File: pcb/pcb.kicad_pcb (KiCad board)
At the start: 2 copper layers, 57 parts, among them J1 AMT0440007DB0000G, J10 Conn_02x10_Counter_Clockwise, J11 Conn_01x03, J12 Conn_01x02, J15 Conn_01x10, J16 Conn_01x10, J2 AMT0440007DB0000G, J3 AMT0440007DB0000G, J4 AMT0440007DB0000G, J5 Conn_01x03, J6 Conn_01x03, J7 Conn_01x03, J8 Conn_01x03, J9 Conn_01x03, Q1 IRF9Z34NPBF, Q2 IRF9Z34NPBF, Q3 IRF9Z34NPBF, Q4 IRF9Z34NPBF, Q5 IRF9Z34NPBF, U1 ACS711ELCTR-12AB-T, U2 ACS711ELCTR-12AB-T, U3 ACS711ELCTR-12AB-T, U4 ACS711ELCTR-12AB-T, U5 ACS711ELCTR-12AB-T, U6 TXS0102DCUR, U7 TXS0102DCUR, U8 TXS0102DCUR, U9 NCP718BSNADJT1G

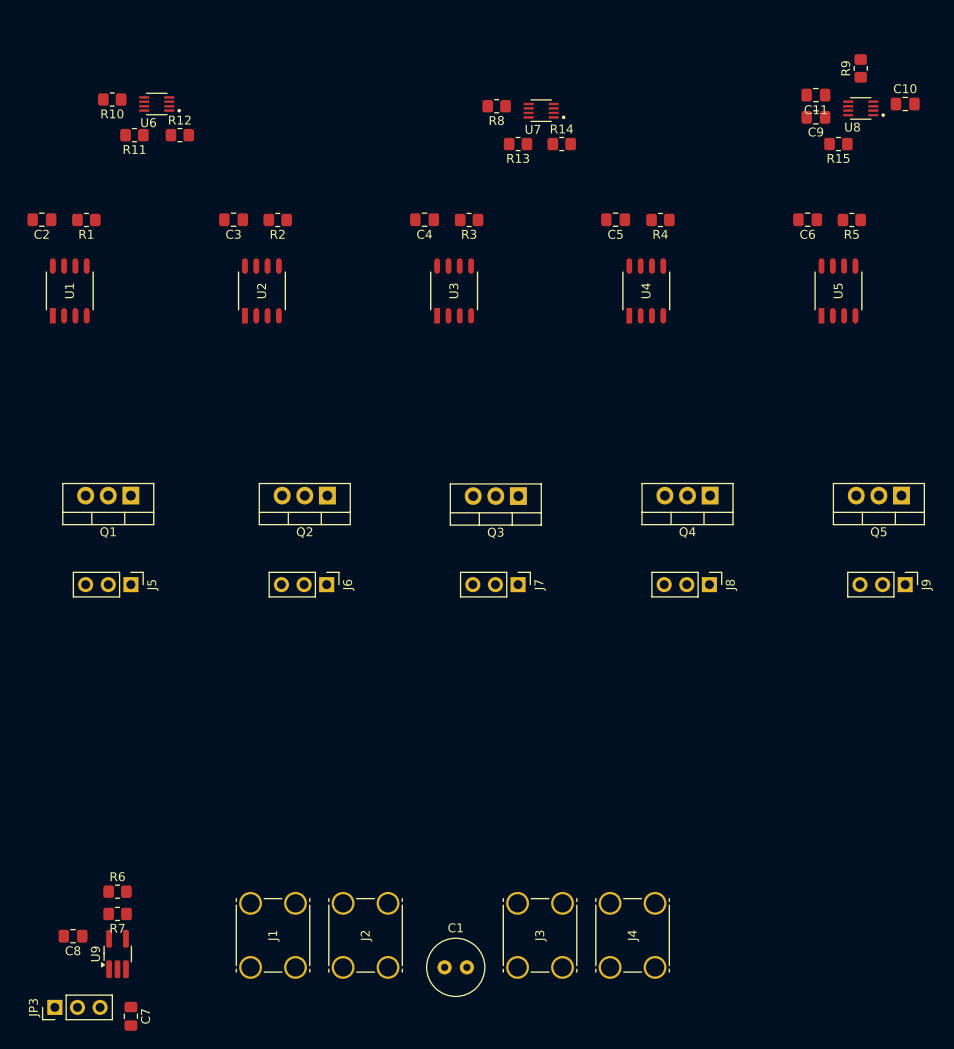
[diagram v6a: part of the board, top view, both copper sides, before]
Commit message: Add bypass capacitors for each level shifter
The datasheet for the level shifter recommends placing the bypass
capacitors as close as possible to the IC. Ideally, we could probably
get away with just the one set. However, since the level shifters are
placed so far away from each other, it's probably better to have more
caps and slightly higher capacicance.
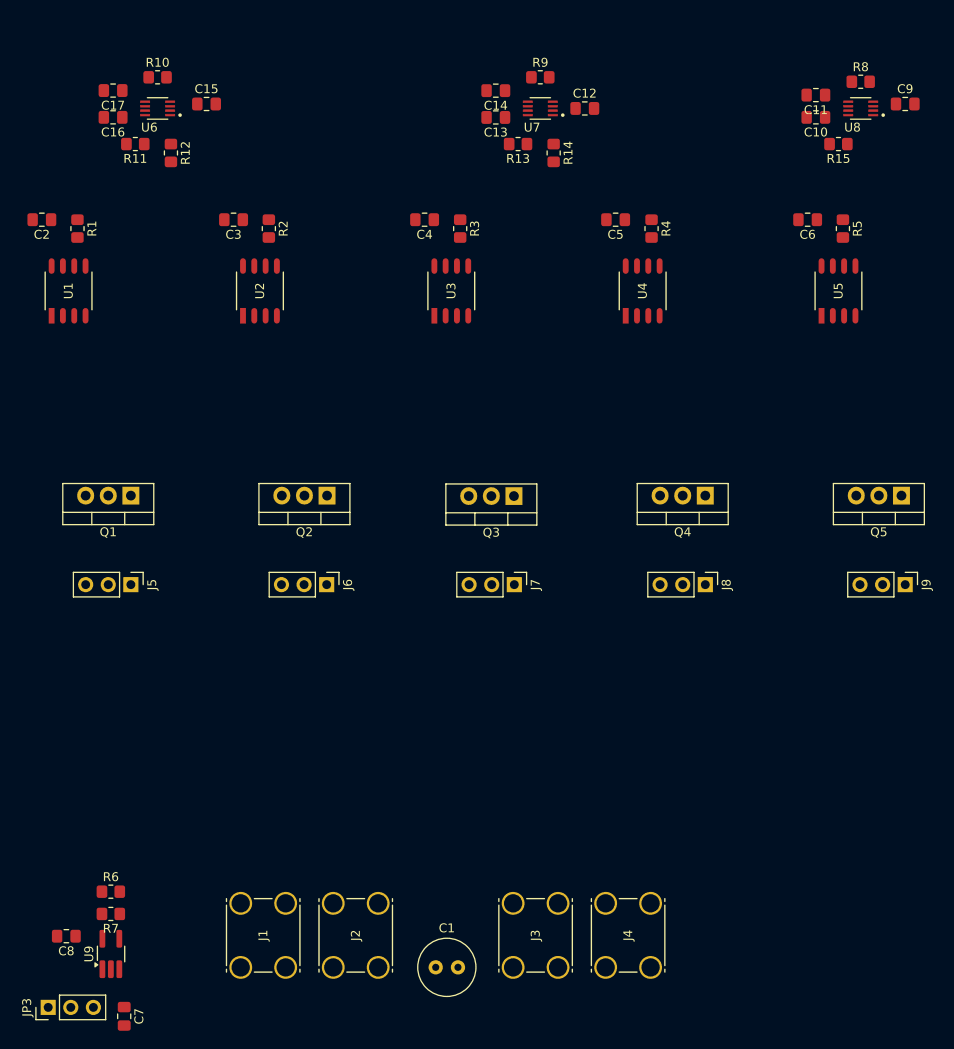
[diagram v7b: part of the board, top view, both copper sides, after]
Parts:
- added C12: 100nF, Capacitor_SMD:C_0805_2012Metric_Pad1.18x1.45mm_HandSolder, F.Cu at (143.0, 81.0)
- added C13: 1µF, Capacitor_SMD:C_0805_2012Metric_Pad1.18x1.45mm_HandSolder, F.Cu at (133.0, 82.0)
- added C14: 100nF, Capacitor_SMD:C_0805_2012Metric_Pad1.18x1.45mm_HandSolder, F.Cu at (133.0, 79.0)
- added C15: 100nF, Capacitor_SMD:C_0805_2012Metric_Pad1.18x1.45mm_HandSolder, F.Cu at (100.5, 80.5)
- added C16: 1µF, Capacitor_SMD:C_0805_2012Metric_Pad1.18x1.45mm_HandSolder, F.Cu at (90.0, 82.0)
- added C17: 100nF, Capacitor_SMD:C_0805_2012Metric_Pad1.18x1.45mm_HandSolder, F.Cu at (90.0, 79.0)
- C10: value 100nF -> 1µF
- C9: value 1µF -> 100nF
- moved R8 41.0 mm to (174.0, 78.0), turned to 0 degrees
- moved R9 36.0 mm to (138.0, 77.5), turned to 0 degrees
- moved C10 10.1 mm to (169.0, 82.0), turned to 180 degrees
- moved C9 10.1 mm to (179.0, 80.5), turned to 0 degrees
- moved R10 5.68 mm to (95.0, 77.5), turned to 0 degrees
- moved R12 2.24 mm to (96.5, 86.0), turned to -90 degrees
- moved R1 1.39 mm to (86.0, 94.5), turned to -90 degrees
- moved R2 1.39 mm to (107.5, 94.5), turned to -90 degrees
- moved R3 1.39 mm to (129.0, 94.5), turned to -90 degrees
- moved R4 1.39 mm to (150.5, 94.5), turned to -90 degrees
- moved R5 1.39 mm to (172.0, 94.5), turned to -90 degrees
- moved R14 1.35 mm to (139.5, 86.0), turned to -90 degrees
- moved J2 1.10 mm to (114.7, 177.5)
- moved J1 1.10 mm to (104.3, 177.5)
- moved R11 1.00 mm to (92.5, 85.0)
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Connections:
- C10 pad 1: +3V3 -> +5V
- C9 pad 1: +5V -> +3V3

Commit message: Change 2x10 headers to use odd-even symbol
The default footprint uses the odd-even pinout, but the schematic was
drawn with a counter clockwise pinout. The pin numbers in the schematic
are arbitrary, so changing the symbol was easier than changing the
footprint pinout to match the counter clockwise symbol.
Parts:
- J10: value Conn_02x10_Counter_Clockwise -> Conn_02x10_Odd_Even
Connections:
- J10 pad 10: SHUTOFF_HAND_L -> I_SENSE_HAND
- J10 pad 11: GNDREF -> SHUTOFF_HIP_L
- J10 pad 12: +3V3 -> Net-(J10-Pin_12)
- J10 pad 13: UART_STM_TX -> SHUTOFF_SHOULDER_L
- J10 pad 15: Net-(J10-Pin_15) -> SHUTOFF_ELBOW_L
- J10 pad 16: I_SENSE_HAND -> UART_STM_TX
- J10 pad 17: I_SENSE_WRIST -> SHUTOFF_WRIST_L
- J10 pad 18: I_SENSE_ELBOW -> +3V3
- J10 pad 19: I_SENSE_SHOULDER -> SHUTOFF_HAND_L
- J10 pad 2: CTRL_HAND -> I_SENSE_HIP
- J10 pad 20: I_SENSE_HIP -> GNDREF
- J10 pad 3: CTRL_ELBOW -> CTRL_HAND
- J10 pad 4: CTRL_WRIST -> I_SENSE_SHOULDER
- J10 pad 5: CTRL_SHOULDER -> CTRL_ELBOW
- J10 pad 6: SHUTOFF_HIP_L -> I_SENSE_ELBOW
- J10 pad 7: SHUTOFF_SHOULDER_L -> CTRL_WRIST
- J10 pad 8: SHUTOFF_ELBOW_L -> I_SENSE_WRIST
- J10 pad 9: SHUTOFF_WRIST_L -> CTRL_SHOULDER
- JP1 pad 1: Net-(J10-Pin_15) -> Net-(J10-Pin_12)
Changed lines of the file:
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@@
 			)
 		)
-		(property "Value" "Conn_02x10_Counter_Clockwise"
+		(property "Value" "Conn_02x10_Odd_Even"
 			(at -1.27 25.63 90)
 			(layer "F.Fab")
@@
 			)
 		)
-		(property "Description" "Generic connector, double row, 02x10, counter clockwise pin numbering scheme (similar to DIP package numbering), script generated (kicad-library-utils/schlib/autogen/connector/)"
+		(property "Description" "Generic connector, double row, 02x10, odd/even pin numbering scheme (row 1 odd numbers, row 2 even numbers), script generated (kicad-library-utils/schlib/autogen/connector/)"
 			(at 0 0 90)
 			(layer "F.Fab")
@@
 			(unit
 				(name "A")
-				(pins "1" "2" "3" "4" "5" "6" "7" "8" "9" "10" "20" "19" "18" "17" "16"
-					"15" "14" "13" "12" "11"
+				(pins "1" "3" "5" "7" "9" "11" "13" "15" "17" "19" "2" "4" "6" "8" "10"
+					"12" "14" "16" "18" "20"
 				)
 			)
@@
 			(layers "*.Cu" "*.Mask")
 			(remove_unused_layers no)
-			(net "CTRL_HAND")
+			(net "I_SENSE_HIP")
 			(pinfunction "Pin_2_2")
 			(pintype "passive")
@@
 			(layers "*.Cu" "*.Mask")
 			(remove_unused_layers no)
-			(net "CTRL_ELBOW")
+			(net "CTRL_HAND")
 			(pinfunction "Pin_3_3")
 			(pintype "passive")
@@
 			(layers "*.Cu" "*.Mask")
 			(remove_unused_layers no)
-			(net "CTRL_WRIST")
+			(net "I_SENSE_SHOULDER")
 			(pinfunction "Pin_4_4")
 			(pintype "passive")
@@
 			(layers "*.Cu" "*.Mask")
 			(remove_unused_layers no)
-			(net "CTRL_SHOULDER")
+			(net "CTRL_ELBOW")
 			(pinfunction "Pin_5_5")
 			(pintype "passive")
@@
 			(layers "*.Cu" "*.Mask")
 			(remove_unused_layers no)
-			(net "SHUTOFF_HIP_L")
+			(net "I_SENSE_ELBOW")
 			(pinfunction "Pin_6_6")
 			(pintype "passive")
@@
 			(layers "*.Cu" "*.Mask")
 			(remove_unused_layers no)
-			(net "SHUTOFF_SHOULDER_L")
+			(net "CTRL_WRIST")
 			(pinfunction "Pin_7_7")
 			(pintype "passive")
@@
 			(layers "*.Cu" "*.Mask")
 			(remove_unused_layers no)
-			(net "SHUTOFF_ELBOW_L")
+			(net "I_SENSE_WRIST")
 			(pinfunction "Pin_8_8")
 			(pintype "passive")
@@
 			(layers "*.Cu" "*.Mask")
 			(remove_unused_layers no)
-			(net "SHUTOFF_WRIST_L")
+			(net "CTRL_SHOULDER")
 			(pinfunction "Pin_9_9")
 			(pintype "passive")
@@
 			(layers "*.Cu" "*.Mask")
 			(remove_unused_layers no)
-			(net "SHUTOFF_HAND_L")
+			(net "I_SENSE_HAND")
 			(pinfunction "Pin_10_10")
 			(pintype "passive")
@@
 			(layers "*.Cu" "*.Mask")
 			(remove_unused_layers no)
-			(net "GNDREF")
+			(net "SHUTOFF_HIP_L")
 			(pinfunction "Pin_11_11")
 			(pintype "passive")
@@
 			(layers "*.Cu" "*.Mask")
 			(remove_unused_layers no)
-			(net "+3V3")
+			(net "Net-(J10-Pin_12)")
 			(pinfunction "Pin_12_12")
-			(pintype "power_out")
+			(pintype "passive")
 		)
 		(pad "13" thru_hole circle
@@
 			(layers "*.Cu" "*.Mask")
 			(remove_unused_layers no)
-			(net "UART_STM_TX")
+			(net "SHUTOFF_SHOULDER_L")
 			(pinfunction "Pin_13_13")
 			(pintype "passive")
@@
 			(layers "*.Cu" "*.Mask")
 			(remove_unused_layers no)
-			(net "Net-(J10-Pin_15)")
+			(net "SHUTOFF_ELBOW_L")
 			(pinfunction "Pin_15_15")
 			(pintype "passive")
@@
 			(layers "*.Cu" "*.Mask")
 			(remove_unused_layers no)
-			(net "I_SENSE_HAND")
+			(net "UART_STM_TX")
 			(pinfunction "Pin_16_16")
 			(pintype "passive")
@@
 			(layers "*.Cu" "*.Mask")
 			(remove_unused_layers no)
-			(net "I_SENSE_WRIST")
+			(net "SHUTOFF_WRIST_L")
 			(pinfunction "Pin_17_17")
 			(pintype "passive")
@@
 			(layers "*.Cu" "*.Mask")
 			(remove_unused_layers no)
-			(net "I_SENSE_ELBOW")
+			(net "+3V3")
 			(pinfunction "Pin_18_18")
 			(pintype "passive")
@@
 			(layers "*.Cu" "*.Mask")
 			(remove_unused_layers no)
-			(net "I_SENSE_SHOULDER")
+			(net "SHUTOFF_HAND_L")
 			(pinfunction "Pin_19_19")
 			(pintype "passive")
@@
 			(layers "*.Cu" "*.Mask")
 			(remove_unused_layers no)
-			(net "I_SENSE_HIP")
+			(net "GNDREF")
 			(pinfunction "Pin_20_20")
 			(pintype "passive")
@@
 			(layers "*.Cu" "*.Mask")
 			(remove_unused_layers no)
-			(net "Net-(J10-Pin_15)")
+			(net "Net-(J10-Pin_12)")
 			(pinfunction "A_1")
 			(pintype "passive")
